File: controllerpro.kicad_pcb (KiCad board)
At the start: 2 copper layers, 92.7 x 33.7 mm, 6 parts

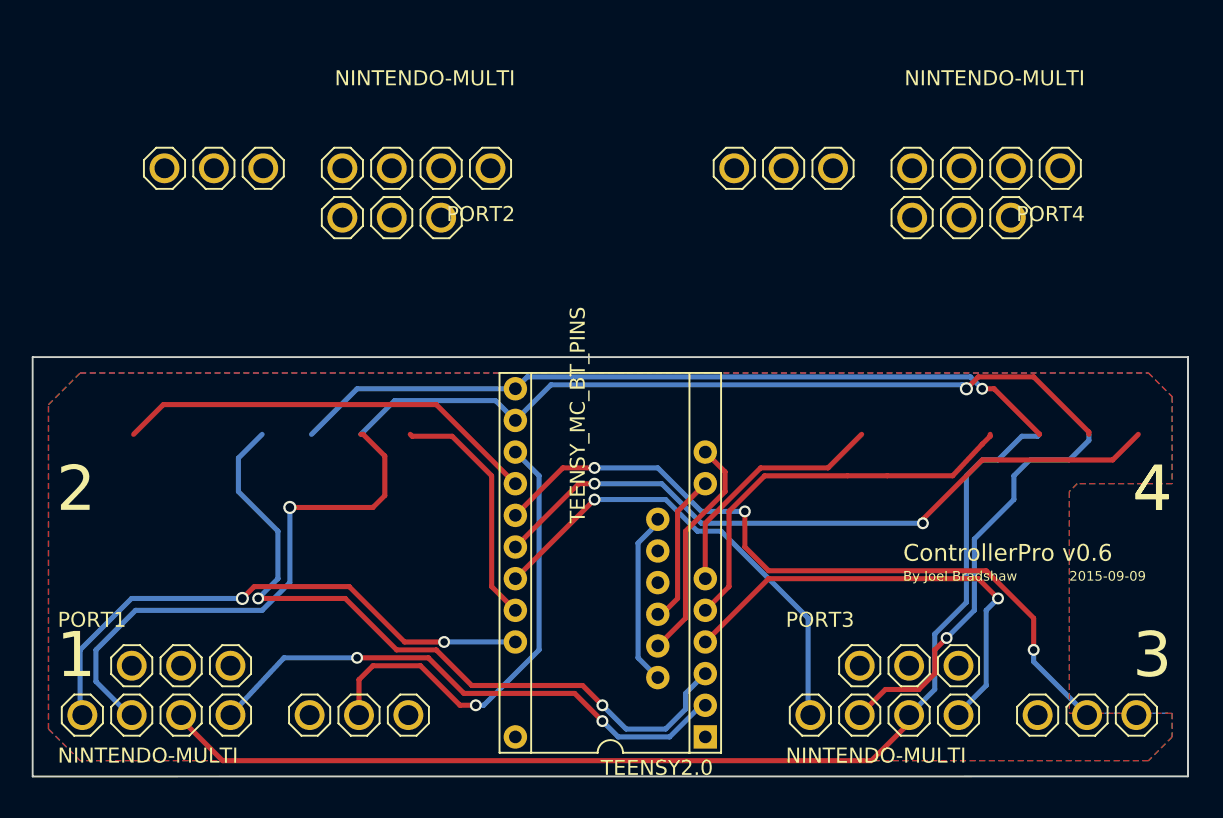
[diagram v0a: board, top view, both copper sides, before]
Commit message: Align board to grid, add border for small board
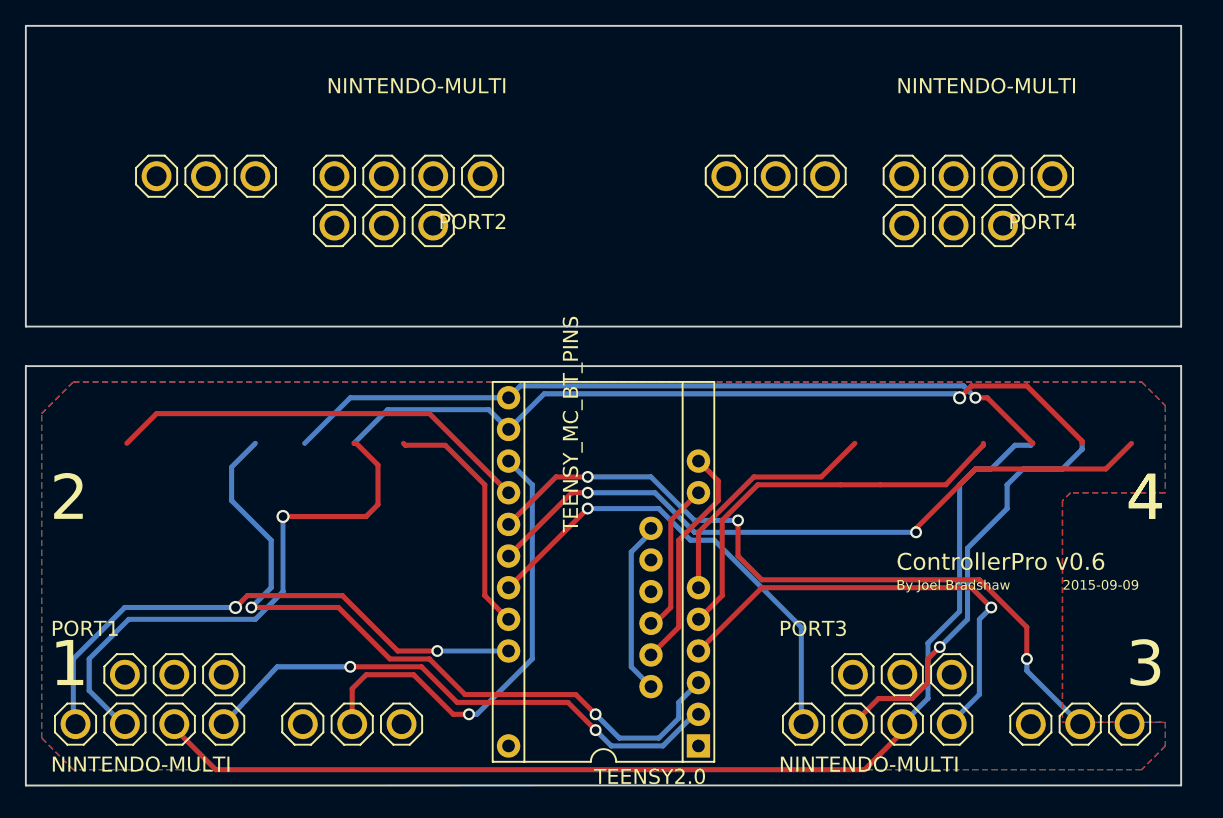
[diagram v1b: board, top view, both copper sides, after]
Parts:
- moved U$1 0.91 mm to (151.8, 108.3)
- moved PORT1 0.91 mm to (117.5, 113.7)
- moved PORT3 0.91 mm to (175.9, 113.7)
- moved TEENSY2.0 0.91 mm to (148.0, 105.4)
- moved PORT2 0.90 mm to (126.4, 73.7)
- moved PORT4 0.90 mm to (172.1, 73.7)
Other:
- board size 92.7 x 33.7 mm -> 92.7 x 61 mm

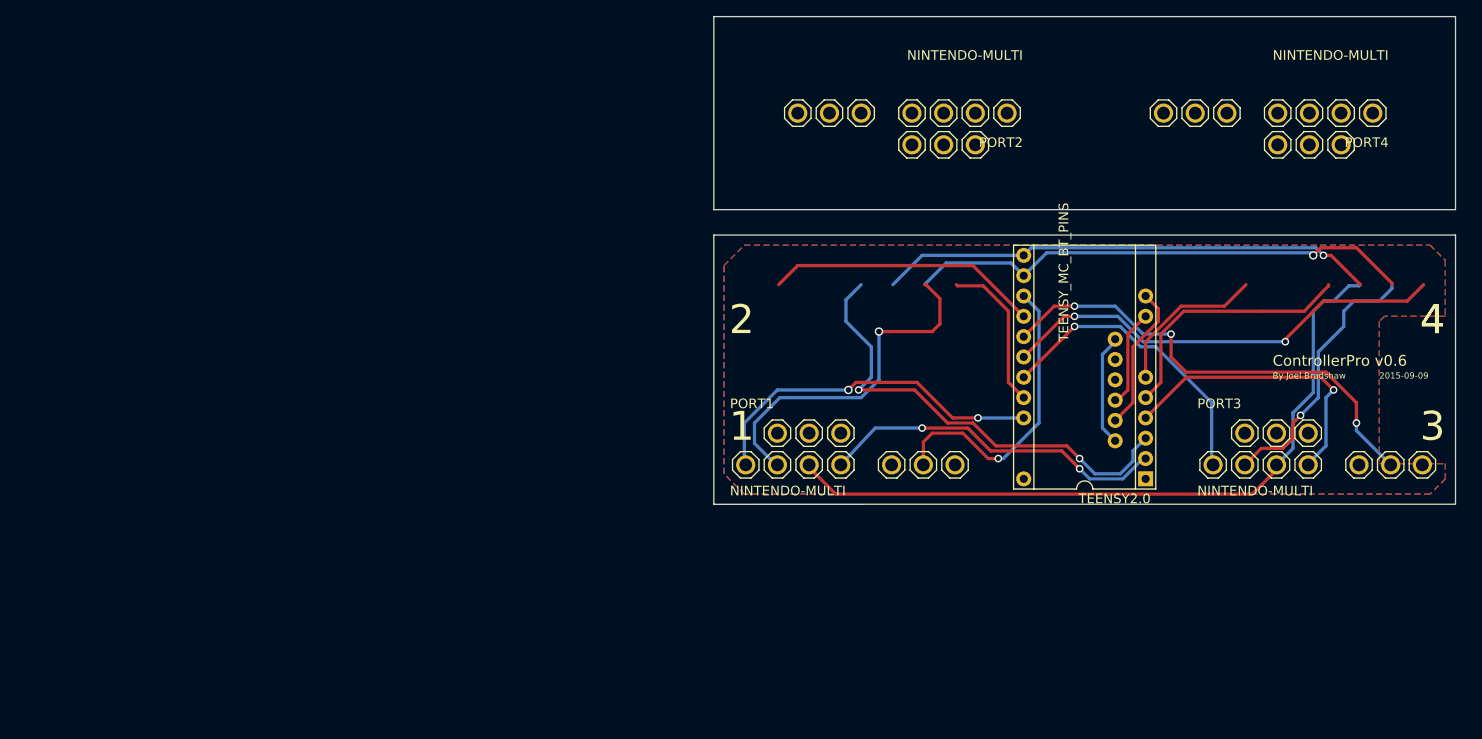
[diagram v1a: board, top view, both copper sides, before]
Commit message: Match footprints and re-label
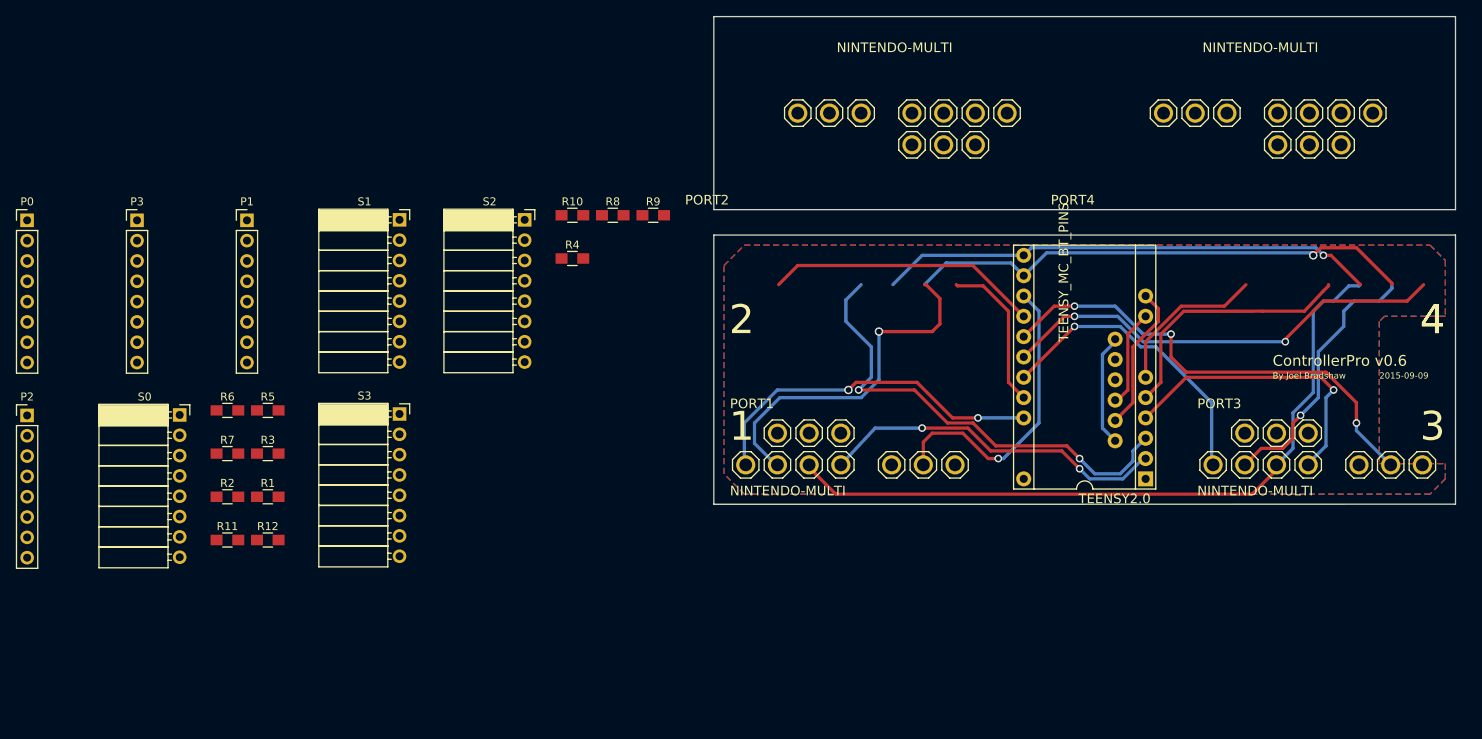
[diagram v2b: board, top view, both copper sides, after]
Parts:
- added P0: Conn_01x08_Male, Pin_Headers:Pin_Header_Straight_1x08_Pitch2.54mm, F.Cu at (15.8, 87.1)
- added P1: Conn_01x08_Male, Pin_Headers:Pin_Header_Straight_1x08_Pitch2.54mm, F.Cu at (43.2, 87.1)
- added P2: Conn_01x08_Male, Pin_Headers:Pin_Header_Straight_1x08_Pitch2.54mm, F.Cu at (15.8, 111.4)
- added P3: Conn_01x08_Male, Pin_Headers:Pin_Header_Straight_1x08_Pitch2.54mm, F.Cu at (29.5, 87.1)
- added R1: R, Resistors_SMD:R_0805_HandSoldering, F.Cu at (45.8, 121.6)
- added R10: R, Resistors_SMD:R_0805_HandSoldering, F.Cu at (83.9, 86.4)
- added R11: R, Resistors_SMD:R_0805_HandSoldering, F.Cu at (40.8, 127.0)
- added R12: R, Resistors_SMD:R_0805_HandSoldering, F.Cu at (45.8, 127.0)
- added R2: R, Resistors_SMD:R_0805_HandSoldering, F.Cu at (40.8, 121.6)
- added R3: R, Resistors_SMD:R_0805_HandSoldering, F.Cu at (45.8, 116.2)
- added R4: R, Resistors_SMD:R_0805_HandSoldering, F.Cu at (83.9, 91.8)
- added R5: R, Resistors_SMD:R_0805_HandSoldering, F.Cu at (45.8, 110.8)
- added R6: R, Resistors_SMD:R_0805_HandSoldering, F.Cu at (40.8, 110.8)
- added R7: R, Resistors_SMD:R_0805_HandSoldering, F.Cu at (40.8, 116.2)
- added R8: R, Resistors_SMD:R_0805_HandSoldering, F.Cu at (89.0, 86.4)
- added R9: R, Resistors_SMD:R_0805_HandSoldering, F.Cu at (94.0, 86.4)
- added S0: Conn_01x08_Female, Socket_Strips:Socket_Strip_Angled_1x08_Pitch2.54mm, F.Cu at (34.8, 111.4)
- added S1: Conn_01x08_Female, Socket_Strips:Socket_Strip_Angled_1x08_Pitch2.54mm, F.Cu at (62.3, 87.0)
- added S2: Conn_01x08_Female, Socket_Strips:Socket_Strip_Angled_1x08_Pitch2.54mm, F.Cu at (78.0, 87.0)
- added S3: Conn_01x08_Female, Socket_Strips:Socket_Strip_Angled_1x08_Pitch2.54mm, F.Cu at (62.3, 111.3)
- PORT2, PORT4: footprint controllerpro:NINTENDO-MULTI -> NINTENDO-MULTI
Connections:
- PORT1 pad 1: S_OR_NES2 -> Net-(PORT1-Pad1)
- PORT1 pad 10: VCC -> Net-(P2-Pad1)
- PORT1 pad 2: CLOCK -> Net-(P2-Pad3)
- PORT1 pad 3: LATCH -> Net-(P2-Pad4)
- PORT1 pad 4: 5VDATA2 -> Net-(P2-Pad5)
- PORT1 pad 5: VCC -> Net-(P2-Pad1)
- PORT1 pad 6: 3VDATA2 -> Net-(P2-Pad7)
- PORT1 pad 7: GND -> Net-(P2-Pad8)
- PORT2 pad 1: S_OR_NES3 -> Net-(PORT2-Pad1)
- PORT2 pad 10: VCC -> Net-(P3-Pad1)
- PORT2 pad 2: CLOCK -> Net-(P3-Pad3)
- PORT2 pad 3: LATCH -> Net-(P3-Pad4)
- PORT2 pad 4: 5VDATA3 -> Net-(P3-Pad5)
- PORT2 pad 5: VCC -> Net-(P3-Pad1)
- PORT2 pad 6: 3VDATA3 -> Net-(P3-Pad7)
- PORT2 pad 7: GND -> Net-(P3-Pad8)
- PORT3 pad 1: S_OR_NES0 -> Net-(PORT3-Pad1)
- PORT3 pad 2: CLOCK -> Net-(P0-Pad3)
- PORT3 pad 3: LATCH -> Net-(P0-Pad4)
- PORT3 pad 4: 5VDATA0 -> Net-(P0-Pad5)
- PORT3 pad 6: 3VDATA0 -> Net-(P0-Pad7)
- PORT3 pad 7: GND -> Net-(P0-Pad8)
- PORT4 pad 1: S_OR_NES1 -> Net-(PORT4-Pad1)
- PORT4 pad 2: CLOCK -> Net-(P1-Pad3)
- PORT4 pad 3: LATCH -> Net-(P1-Pad4)
- PORT4 pad 4: 5VDATA1 -> Net-(P1-Pad5)
- PORT4 pad 6: 3VDATA1 -> Net-(P1-Pad7)
- PORT4 pad 7: GND -> Net-(P1-Pad8)
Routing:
- net CLOCK: track 141.7 -> 63.9 mm, vias 3 -> 1
- net Net-(P2-Pad3): track 0.00 -> 44.2 mm, vias 0 -> 1
- net Net-(P0-Pad3): track 0.00 -> 33.6 mm, vias 0 -> 1

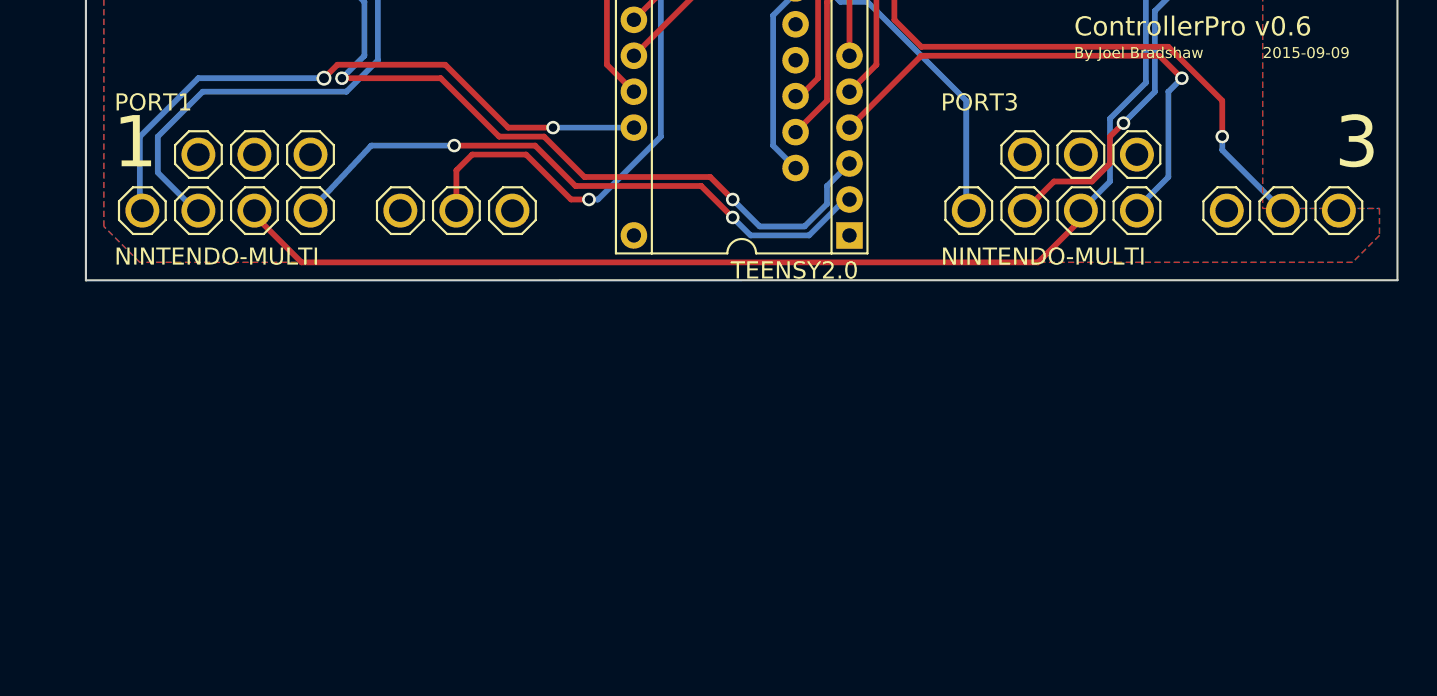
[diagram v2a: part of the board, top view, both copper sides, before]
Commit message: Move second set of multiports
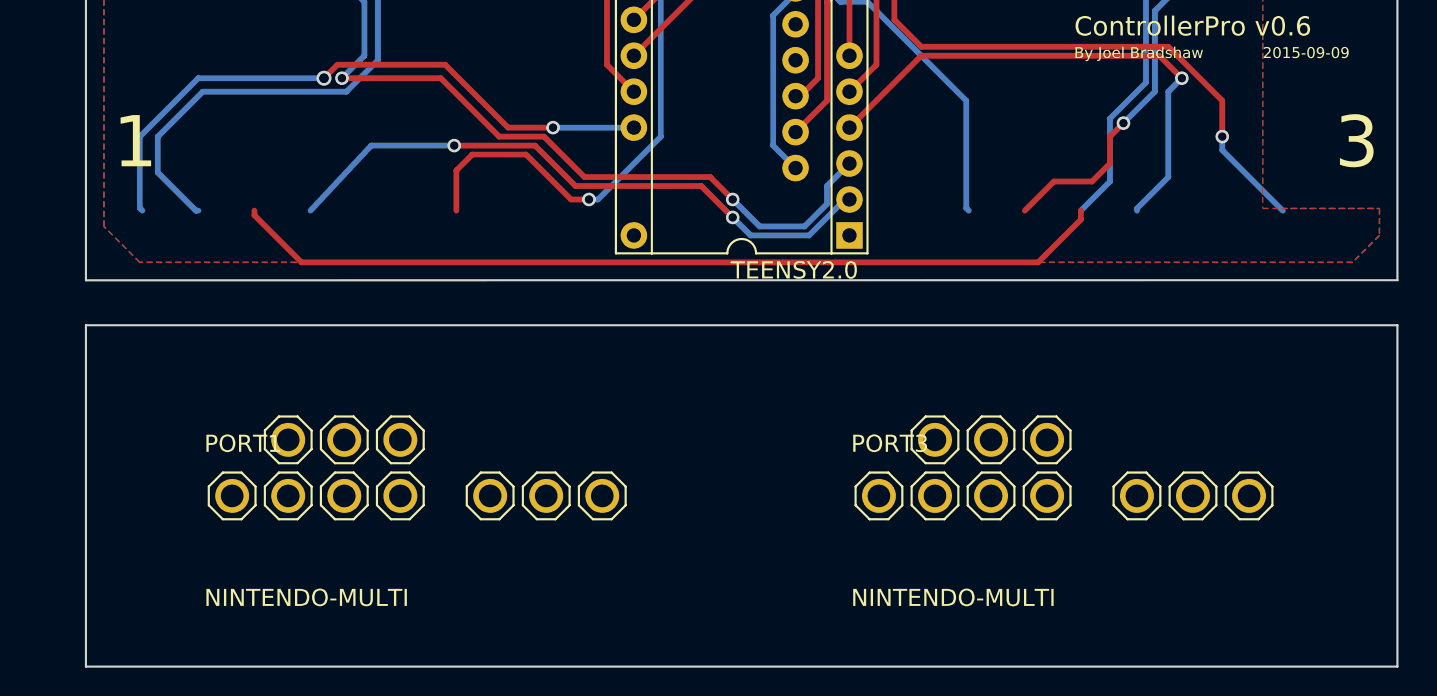
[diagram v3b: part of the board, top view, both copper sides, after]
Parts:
- PORT1, PORT3: footprint NINTENDO-MULTI -> controllerpro:NINTENDO-MULTI
- moved PORT3 25.0 mm to (169.5, 137.8)
- moved PORT1 25.0 mm to (123.8, 137.8)
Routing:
- net LATCH: track 152.6 -> 62.2 mm
- net Net-(P0-Pad4): track 0.00 -> 90.4 mm
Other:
- board size 92.7 x 61 mm -> 92.7 x 88.3 mm

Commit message: Start laying out board
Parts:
- moved P0 157.1 mm to (162.6, 142.9), turned to 90 degrees
- moved P1 137.1 mm to (179.1, 68.6), turned to 270 degrees
- moved R2 116.2 mm to (156.3, 134.0), turned to 180 degrees
- moved R1 110.9 mm to (154.9, 141.6), turned to 90 degrees
- moved R3 108.7 mm to (152.5, 137.2)
- moved P3 105.5 mm to (133.3, 68.6), turned to 270 degrees
- moved P2 105.2 mm to (116.2, 142.9), turned to 90 degrees

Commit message: More layout
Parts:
- P0, P1, P2, P3, R1: moved to B.Cu
- moved R1 2.84 mm to (157.5, 142.9), turned to 180 degrees
- turned P0 to 270 degrees
- turned P1 to 90 degrees
- turned P2 to 270 degrees
- turned P3 to 90 degrees
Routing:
- net VCC: track 0.00 -> 35.1 mm
- net Net-(P0-Pad2): track 0.00 -> 9.65 mm
- net Net-(P0-Pad3): track 33.6 -> 41.7 mm
- net Net-(P0-Pad4): track 90.4 -> 97.4 mm
- net Net-(P0-Pad8): track 0.00 -> 6.52 mm
- net Net-(P0-Pad5): track 0.00 -> 6.40 mm
- net Net-(P0-Pad7): track 0.00 -> 5.93 mm
- net Net-(PORT3-Pad1): track 0.00 -> 5.71 mm

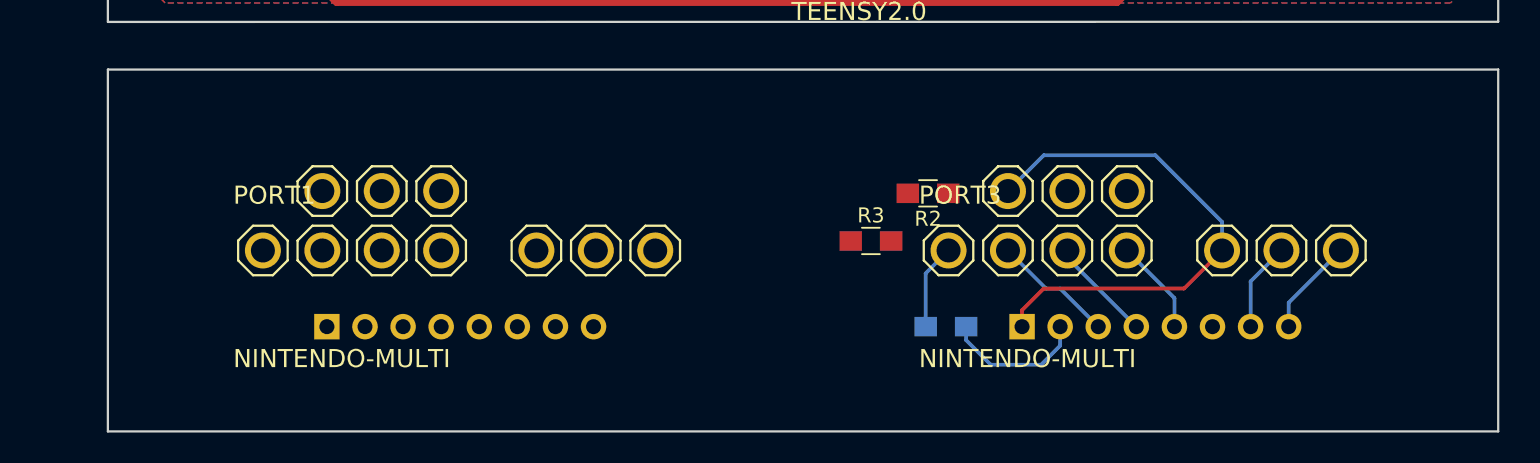
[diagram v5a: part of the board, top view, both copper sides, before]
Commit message: Make it default to configurable SNES/NES
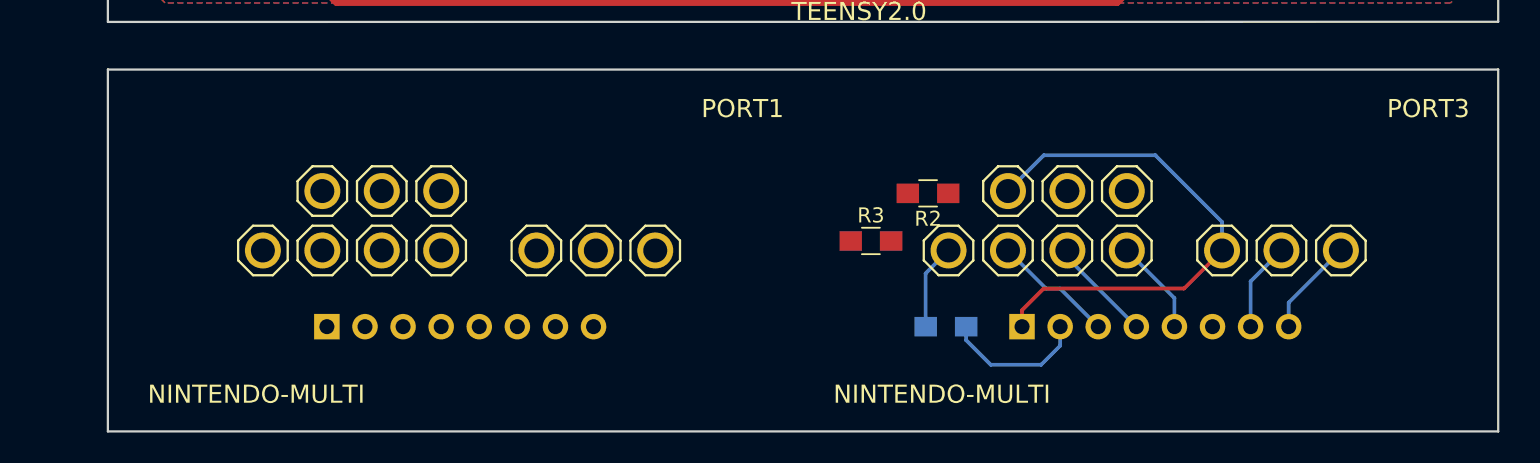
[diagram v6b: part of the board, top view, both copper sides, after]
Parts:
- PORT1, PORT3: footprint controllerpro:NINTENDO-MULTI -> NINTENDO-MULTI
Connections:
- P0 pad 1: VCC -> Net-(P0-Pad1)
- P1 pad 1: VCC -> Net-(P1-Pad1)
- PORT3 pad 10: VCC -> Net-(P0-Pad1)
- PORT3 pad 5: VCC -> Net-(P0-Pad1)
- PORT4 pad 10: VCC -> Net-(P1-Pad1)
- PORT4 pad 5: VCC -> Net-(P1-Pad1)
- R2 pad 1: VCC -> Net-(P0-Pad1)
- R5 pad 1: VCC -> Net-(P1-Pad1)
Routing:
- net VCC: track 35.1 -> 0.00 mm
- net Net-(P0-Pad1): track 0.00 -> 35.1 mm
